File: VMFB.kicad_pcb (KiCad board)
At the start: 2 copper layers, 141.6 x 109.9 mm, 110 parts, among them J1 Barrel_Jack_Switch, J10 Conn_01x03_Pin, J11 Conn_01x06_Pin, J12 Conn_01x04_Pin, J13 Conn_01x04_Pin, J14 Conn_01x04_Pin, J2 USB_B, J3 Screw_Terminal_01x02, J4 Screw_Terminal_01x03, J5 Conn_01x03_Pin, J6 Conn_01x04_Pin, J7 Conn_01x04_Pin, J8 Conn_01x04_Pin, J9 Conn_01x02_Pin, Q1 BC547, Q2 BC547, Q3 BC547, Q4 BD139, Q5 TIP41C, Q6 BC547, U1 LM358, U2 NE555P, U3 NE555P, U4 NE555P, U5 NE555P

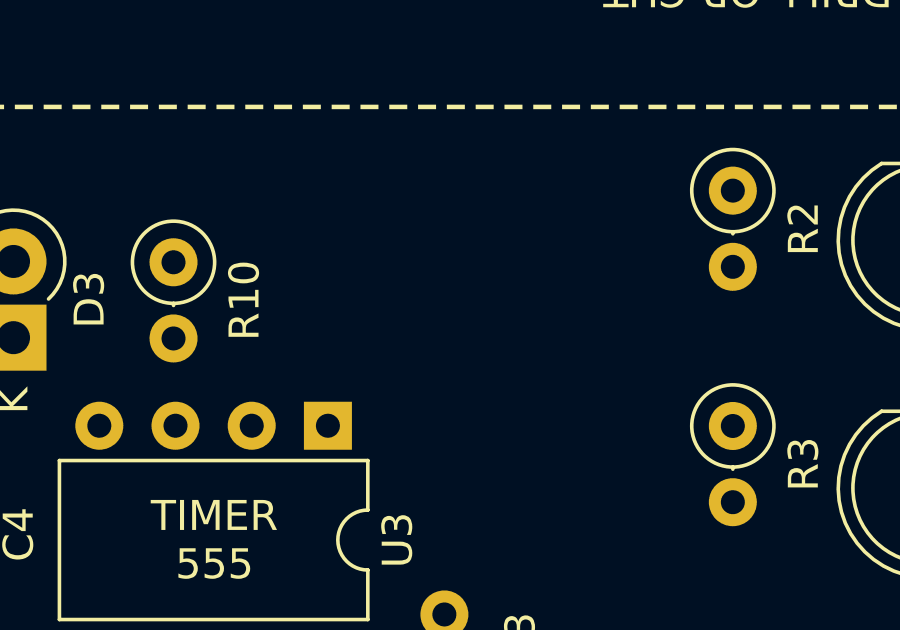
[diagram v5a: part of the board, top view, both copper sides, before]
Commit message: added resistor and diode to turn IR LEDs on when the timer triggers so the dispense sensors can stop the motor
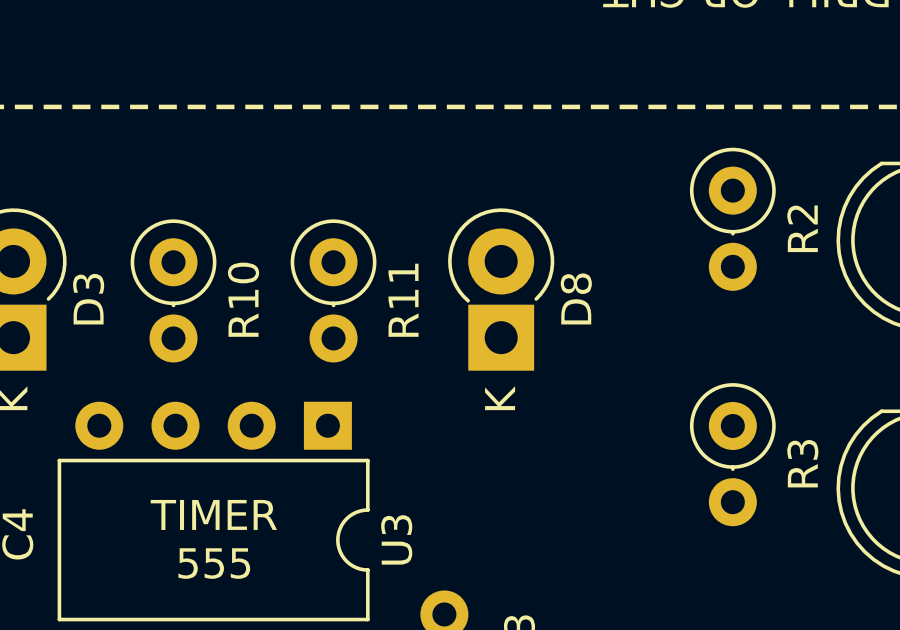
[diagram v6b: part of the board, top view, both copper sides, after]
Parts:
- added D8: 1N4007, Diode_THT:D_DO-41_SOD81_P2.54mm_Vertical_KathodeUp, F.Cu at (189.0, 47.7)
- added R11: 10K, Resistor_THT:R_Axial_DIN0207_L6.3mm_D2.5mm_P2.54mm_Vertical, F.Cu at (183.4, 45.2)
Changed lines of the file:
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@@
   (net 77 "Net-(D3-A)")
   (net 78 "Net-(Q5-B)")
+  (net 79 "Net-(D8-A)")
   (footprint "Resistor_THT:R_Axial_DIN0207_L6.3mm_D2.5mm_P2.54mm_Vertical" (layer "F.Cu")
     (at 114.6332 65.5474 90)
@@
       (net 72 "Net-(D7-A)") (pintype "passive"))
     (model "${KICAD6_3DMODEL_DIR}/Resistor_THT.3dshapes/R_Axial_DIN0207_L6.3mm_D2.5mm_P2.54mm_Vertical.wrl"
+      (offset (xyz 0 0 0))
+      (scale (xyz 1 1 1))
+      (rotate (xyz 0 0 0))
+    )
+  )
+  (footprint "Diode_THT:D_DO-41_SOD81_P2.54mm_Vertical_KathodeUp" (layer "F.Cu")
+    (at 188.976 47.696234 90)
+    (descr "Diode, DO-41_SOD81 series, Axial, Vertical, pin pitch=2.54mm, , length*diameter=5.2*2.7mm^2, , http://www.diodes.com/_files/packages/DO-41%20(Plastic).pdf")
+    (tags "Diode DO-41_SOD81 series Axial Vertical pin pitch 2.54mm  length 5.2mm diameter 2.7mm")
+    (property "Sheetfile" "VMFB.kicad_sch")
+    (property "Sheetname" "")
+    (property "Sim.Device" "D")
+    (property "Sim.Pins" "1=K 2=A")
+    (property "ki_description" "1000V 1A General Purpose Rectifier Diode, DO-41")
+    (property "ki_keywords" "diode")
+    (attr through_hole)
+    (fp_text reference "D8" (at 1.27 2.54 90) (layer "F.SilkS")
+        (effects (font (size 1 1) (thickness 0.15)))
+    )
+    (fp_text value "1N4007" (at 1.27 3.639635 90) (layer "F.Fab")
+        (effects (font (size 1 1) (thickness 0.15)))
+    )
+    (fp_text user "K" (at -2.1 0 90) (layer "F.SilkS")
+        (effects (font (size 1 1) (thickness 0.15)))
+    )
+    (fp_text user "K" (at -2.1 0 90) (layer "F.Fab")
+        (effects (font (size 1 1) (thickness 0.15)))
+    )
+    (fp_text user "${REFERENCE}" (at 1.27 -2.750635 90) (layer "F.Fab")
+        (effects (font (size 1 1) (thickness 0.15)))
+    )
+    (fp_arc (start 1.228847 -1.1) (mid 4.250877 -0.044974) (end 1.288449 1.167366)
+      (stroke (width 0.12) (type solid)) (layer "F.SilkS"))
+    (fp_line (start -1.35 -1.6) (end -1.35 1.6)
+      (stroke (width 0.05) (type solid)) (layer "F.CrtYd"))
+    (fp_line (start -1.35 1.6) (end 4.15 1.6)
+      (stroke (width 0.05) (type solid)) (layer "F.CrtYd"))
+    (fp_line (start 4.15 -1.6) (end -1.35 -1.6)
+      (stroke (width 0.05) (type solid)) (layer "F.CrtYd"))
+    (fp_line (start 4.15 1.6) (end 4.15 -1.6)
+      (stroke (width 0.05) (type solid)) (layer "F.CrtYd"))
+    (fp_line (start 0 0) (end 2.54 0)
+      (stroke (width 0.1) (type solid)) (layer "F.Fab"))
+    (fp_circle (center 2.54 0) (end 3.89 0)
+      (stroke (width 0.1) (type solid)) (fill none) (layer "F.Fab"))
+    (pad "1" thru_hole rect (at 0 0 90) (size 2.2 2.2) (drill 1.1) (layers "*.Cu" "*.Mask")
+      (net 73 "PIR MON") (pinfunction "K") (pintype "passive"))
+    (pad "2" thru_hole oval (at 2.54 0 90) (size 2.2 2.2) (drill 1.1) (layers "*.Cu" "*.Mask")
+      (net 79 "Net-(D8-A)") (pinfunction "A") (pintype "passive"))
+    (model "${KICAD6_3DMODEL_DIR}/Diode_THT.3dshapes/D_DO-41_SOD81_P2.54mm_Vertical_KathodeUp.wrl"
       (offset (xyz 0 0 0))
       (scale (xyz 1 1 1))
@@
       (offset (xyz 0 0 0))
       (scale (xyz 1 1 1))
+      (rotate (xyz 0 0 0))
+    )
+  )
+  (footprint "Resistor_THT:R_Axial_DIN0207_L6.3mm_D2.5mm_P2.54mm_Vertical" (layer "F.Cu")
+    (at 183.388 45.183 -90)
+    (descr "Resistor, Axial_DIN0207 series, Axial, Vertical, pin pitch=2.54mm, 0.25W = 1/4W, length*diameter=6.3*2.5mm^2, http://cdn-reichelt.de/documents/datenblatt/B400/1_4W%23YAG.pdf")
+    (tags "Resistor Axial_DIN0207 series Axial Vertical pin pitch 2.54mm 0.25W = 1/4W length 6.3mm diameter 2.5mm")
+    (property "Sheetfile" "VMFB.kicad_sch")
+    (property "Sheetname" "")
+    (property "ki_description" "Resistor")
+    (property "ki_keywords" "R res resistor")
+    (attr through_hole)
+    (fp_text reference "R11" (at 1.27 -2.37 90) (layer "F.SilkS")
+        (effects (font (size 1 1) (thickness 0.15)))
+    )
+    (fp_text value "10K" (at 1.27 2.37 90) (layer "F.Fab")
+        (effects (font (size 1 1) (thickness 0.15)))
+    )
+    (fp_text user "${REFERENCE}" (at 1.27 -2.37 90) (layer "F.Fab")
+        (effects (font (size 1 1) (thickness 0.15)))
+    )
+    (fp_line (start 1.37 0) (end 1.44 0)
+      (stroke (width 0.12) (type solid)) (layer "F.SilkS"))
+    (fp_circle (center 0 0) (end 1.37 0)
+      (stroke (width 0.12) (type solid)) (fill none) (layer "F.SilkS"))
+    (fp_line (start -1.5 -1.5) (end -1.5 1.5)
+      (stroke (width 0.05) (type solid)) (layer "F.CrtYd"))
+    (fp_line (start -1.5 1.5) (end 3.59 1.5)
+      (stroke (width 0.05) (type solid)) (layer "F.CrtYd"))
+    (fp_line (start 3.59 -1.5) (end -1.5 -1.5)
+      (stroke (width 0.05) (type solid)) (layer "F.CrtYd"))
+    (fp_line (start 3.59 1.5) (end 3.59 -1.5)
+      (stroke (width 0.05) (type solid)) (layer "F.CrtYd"))
+    (fp_line (start 0 0) (end 2.54 0)
+      (stroke (width 0.1) (type solid)) (layer "F.Fab"))
+    (fp_circle (center 0 0) (end 1.25 0)
+      (stroke (width 0.1) (type solid)) (fill none) (layer "F.Fab"))
+    (pad "1" thru_hole circle (at 0 0 270) (size 1.6 1.6) (drill 0.8) (layers "*.Cu" "*.Mask")
+      (net 79 "Net-(D8-A)") (pintype "passive"))
+    (pad "2" thru_hole oval (at 2.54 0 270) (size 1.6 1.6) (drill 0.8) (layers "*.Cu" "*.Mask")
+      (net 47 "Net-(U3-Q)") (pintype "passive"))
+    (model "${KICAD6_3DMODEL_DIR}/Resistor_THT.3dshapes/R_Axial_DIN0207_L6.3mm_D2.5mm_P2.54mm_Vertical.wrl"
+      (offset (xyz 0 0 0))
+      (scale (xyz 1 1 1))

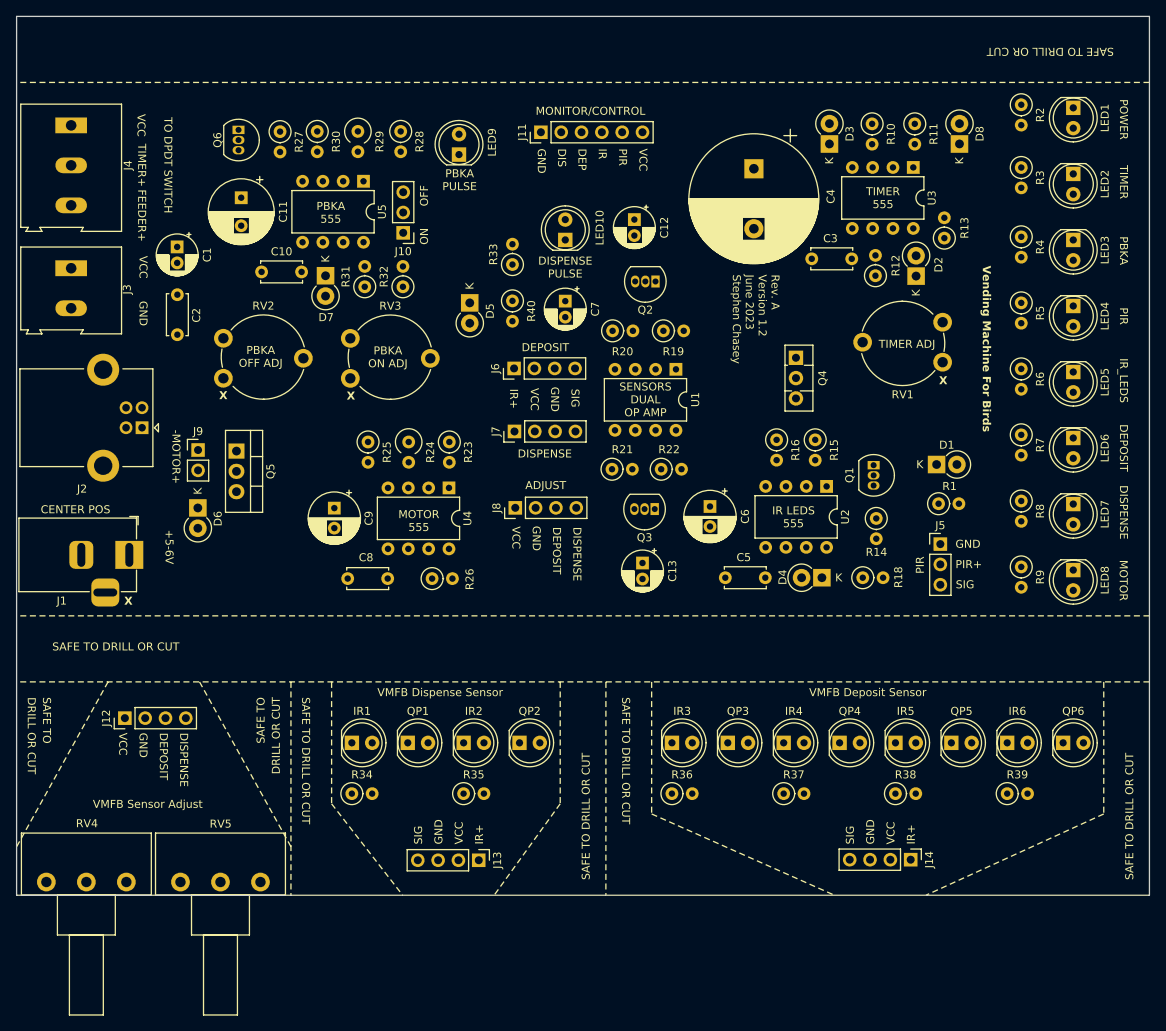
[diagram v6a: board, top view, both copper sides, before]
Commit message: a few small tweaks, connecting the switch pin of the barrel jack to ground
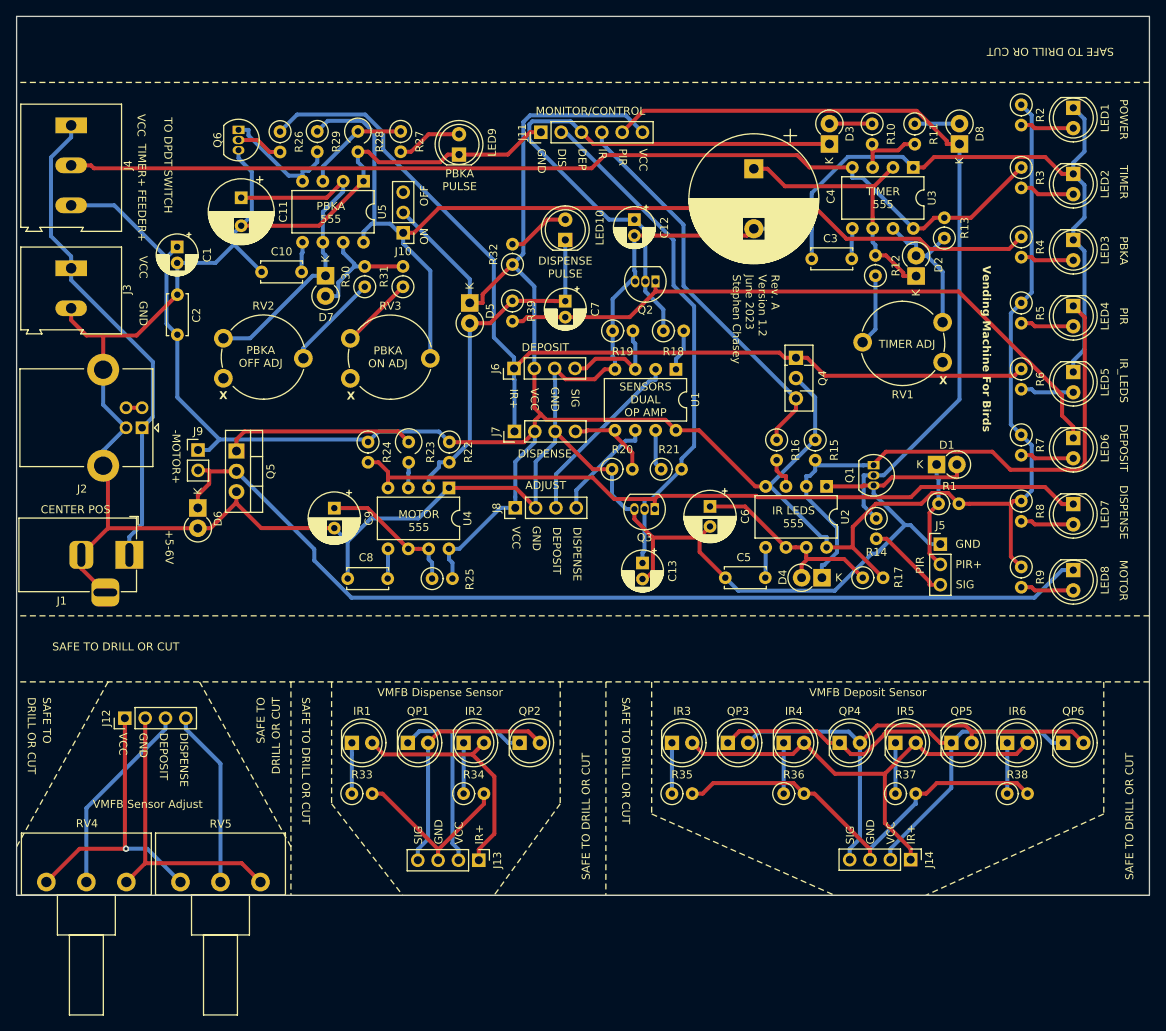
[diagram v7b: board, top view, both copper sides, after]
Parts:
- R17: renamed from R18; value 470K -> 220K
- renumbered R19 to R18, R20 to R19, R21 to R20, R22 to R21, R23 to R22, R24 to R23, R25 to R24, R26 to R25, R27 to R26, R28 to R27, R29 to R28, R30 to R29, R31 to R30, R32 to R31, R33 to R32, R34 to R33, R35 to R34, R36 to R35, R37 to R36, R38 to R37, R39 to R38, R40 to R39
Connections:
- J1 pad 3: unconnected-(J1-Pad3) -> GND
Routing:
- net GND: track 0.00 -> 445.3 mm
- net VCC: track 0.00 -> 347.3 mm
- net TIMER+: track 0.00 -> 127.3 mm
- net Net-(J10-Pin_1): track 0.00 -> 125.4 mm
- net IR+: track 0.00 -> 124.6 mm
- net Net-(D6-K): track 0.00 -> 123.5 mm
- net PIR MON: track 0.00 -> 99.1 mm
- net MOTOR RESET: track 0.00 -> 94.7 mm
- net Net-(LED6-K): track 0.00 -> 82.8 mm
- net Net-(D4-K): track 0.00 -> 74.0 mm
- net DEPOSIT MON: track 0.00 -> 73.4 mm
- net Net-(J14-Pin_2): track 0.00 -> 64.4 mm
- net DISPENSE MON: track 0.00 -> 64.3 mm
- net Net-(J14-Pin_4): track 0.00 -> 61.4 mm
- net Net-(J2-VBUS): track 0.00 -> 61.2 mm
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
